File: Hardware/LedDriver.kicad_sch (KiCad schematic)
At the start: 10 parts

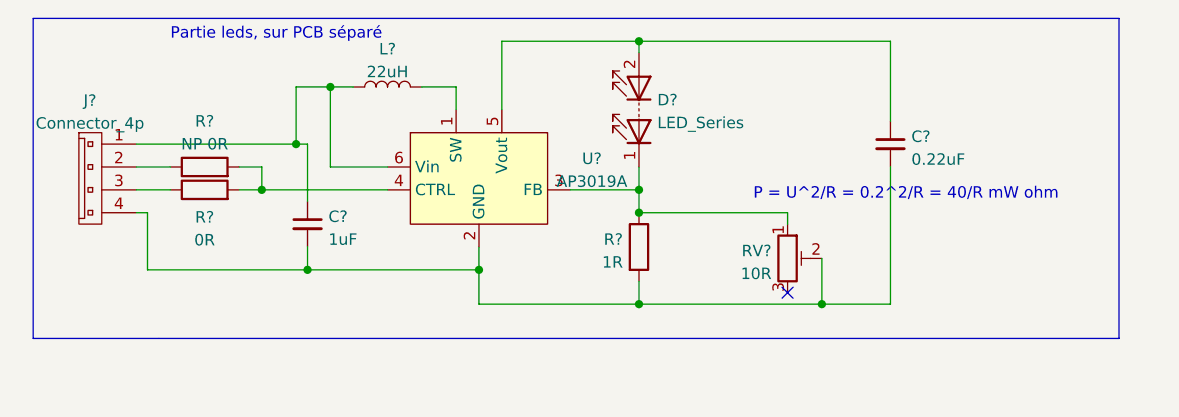
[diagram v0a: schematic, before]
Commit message: pcb led driver
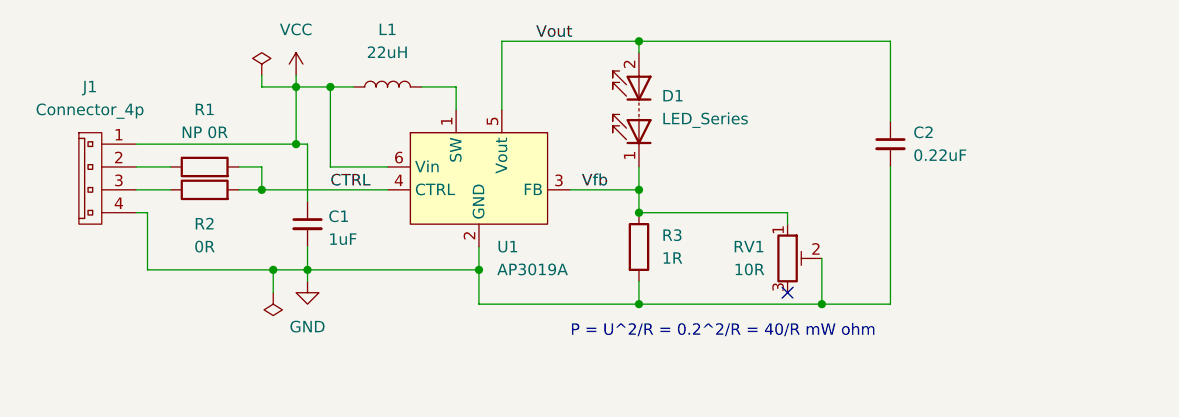
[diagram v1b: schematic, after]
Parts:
- C1, C2: renamed from C?; footprint (none) -> 0ESNLib:C_0805_2012Metric_Pad1.18x1.45mm_HandSolder
- D1: renamed from D?; footprint (none) -> 0ESNLib:D_0603_1608Metric_Pad1.05x0.95mm_HandSolder
- L1: renamed from L?; footprint (none) -> 0ESNLib:sumida_CDRH_inductor
- R1, R2, R3: renamed from R?; footprint (none) -> Resistor_SMD:R_0805_2012Metric_Pad1.20x1.40mm_HandSolder
- U1: renamed from U?; footprint (none) -> Package_TO_SOT_SMD:TSOT-23-6_HandSoldering
- gave numbers to parts that had none: 2
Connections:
- net Vfb: now reaches D1.1 (K), R3.1, RV1.1, U1.3 (FB)
- net GND: now reaches C1.2, C2.2, J1.4 (P4), R3.2, RV1.2, U1.2 (GND)
- net CTRL: now reaches R1.2, R2.2, U1.4 (CTRL)
- net Vout: now reaches C2.1, D1.2 (A), U1.5 (Vout)
- net VCC: now reaches C1.1, J1.1 (P1), L1.1, U1.6 (Vin)
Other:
- note removed: "Partie leds, sur PCB séparé"

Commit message: edited libraries
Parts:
- J1: value Connector_4p -> Led connector; footprint 0ESN_Lib:Connector_2p_m -> 0ESN_Lib:Connector_4p_m
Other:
- note added: "EN"
- note added: "GND"
- note added: "PWM"
- note added: "Vbat"
- moved on the sheet: C1, C2, D1, L1, R1, R2, R3, RV1, U1

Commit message: led driver schematic done
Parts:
- C1, C2: footprint 0ESNLib:C_0805_2012Metric_Pad1.18x1.45mm_HandSolder -> 0ESN_Lib:C_0805_2012Metric_Pad1.18x1.45mm_HandSolder
- D1: footprint 0ESNLib:D_0603_1608Metric_Pad1.05x0.95mm_HandSolder -> 0ESN_Lib:C_0805_2012Metric_Pad1.18x1.45mm_HandSolder
- L1: footprint 0ESNLib:sumida_CDRH_inductor -> 0ESN_Lib:sumida_CDRH_inductor
- RV1: footprint (none) -> 0ESN_Lib:Bourns_3362p_trimpot
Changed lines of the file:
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@@
       (effects (font (size 1.27 1.27)) (justify right))
     )
-    (property "Footprint" "" (id 2) (at 182.88 107.95 0)
+    (property "Footprint" "0ESN_Lib:Bourns_3362p_trimpot" (id 2) (at 182.88 107.95 0)
       (effects (font (size 1.27 1.27)) hide)
     )
@@
     (property "Reference" "L1" (id 0) (at 139.7 83.82 90))
     (property "Value" "22uH" (id 1) (at 139.7 86.36 90))
-    (property "Footprint" "0ESNLib:sumida_CDRH_inductor" (id 2) (at 139.7 90.17 0)
+    (property "Footprint" "0ESN_Lib:sumida_CDRH_inductor" (id 2) (at 139.7 90.17 0)
       (effects (font (size 1.27 1.27)) hide)
     )
@@
       (effects (font (size 1.27 1.27)) (justify right))
     )
-    (property "Footprint" "0ESNLib:D_0603_1608Metric_Pad1.05x0.95mm_HandSolder" (id 2) (at 166.37 95.25 0)
+    (property "Footprint" "0ESN_Lib:C_0805_2012Metric_Pad1.18x1.45mm_HandSolder" (id 2) (at 166.37 95.25 0)
       (effects (font (size 1.27 1.27)) hide)
     )
@@
       (effects (font (size 1.27 1.27)) (justify left))
     )
-    (property "Footprint" "0ESNLib:C_0805_2012Metric_Pad1.18x1.45mm_HandSolder" (id 2) (at 129.54 105.41 0)
+    (property "Footprint" "0ESN_Lib:C_0805_2012Metric_Pad1.18x1.45mm_HandSolder" (id 2) (at 129.54 105.41 0)
       (effects (font (size 1.27 1.27)) hide)
     )
@@
       (effects (font (size 1.27 1.27)) (justify left))
     )
-    (property "Footprint" "0ESNLib:C_0805_2012Metric_Pad1.18x1.45mm_HandSolder" (id 2) (at 194.31 100.33 0)
+    (property "Footprint" "0ESN_Lib:C_0805_2012Metric_Pad1.18x1.45mm_HandSolder" (id 2) (at 194.31 100.33 0)
       (effects (font (size 1.27 1.27)) hide)
     )
@@
     )
     (path "/be7fe3ef-4c8c-4441-a8b1-9f6c4a556dbd"
-      (reference "C1") (unit 1) (value "1uF") (footprint "0ESNLib:C_0805_2012Metric_Pad1.18x1.45mm_HandSolder")
+      (reference "C1") (unit 1) (value "1uF") (footprint "0ESN_Lib:C_0805_2012Metric_Pad1.18x1.45mm_HandSolder")
     )
     (path "/cabd8106-febf-4c1c-a427-4a77d8f3282a"
-      (reference "C2") (unit 1) (value "0.22uF") (footprint "0ESNLib:C_0805_2012Metric_Pad1.18x1.45mm_HandSolder")
+      (reference "C2") (unit 1) (value "0.22uF") (footprint "0ESN_Lib:C_0805_2012Metric_Pad1.18x1.45mm_HandSolder")
     )
     (path "/b9fa4c1e-5267-4696-a1ce-f87e6baeeb29"
-      (reference "D1") (unit 1) (value "LED_Series") (footprint "0ESNLib:D_0603_1608Metric_Pad1.05x0.95mm_HandSolder")
+      (reference "D1") (unit 1) (value "LED_Series") (footprint "0ESN_Lib:C_0805_2012Metric_Pad1.18x1.45mm_HandSolder")
     )
     (path "/e4ceb904-3dd0-416a-906e-cac55e2455db"
@@
     )
     (path "/9c08c45f-ba32-4b2b-8fe9-de49dcdc4262"
-      (reference "L1") (unit 1) (value "22uH") (footprint "0ESNLib:sumida_CDRH_inductor")
+      (reference "L1") (unit 1) (value "22uH") (footprint "0ESN_Lib:sumida_CDRH_inductor")
     )
     (path "/a5b92ca1-98a4-4608-b742-8ab56d6b3726"
@@
     )
     (path "/0229117d-4c4e-4f89-956e-fd71503672e7"
-      (reference "RV1") (unit 1) (value "10R") (footprint "")
+      (reference "RV1") (unit 1) (value "10R") (footprint "0ESN_Lib:Bourns_3362p_trimpot")
     )
     (path "/17354649-0d95-44b1-afcb-6c3c12f701a5"

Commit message: led driver pcb complete
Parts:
- D1: footprint 0ESN_Lib:C_0805_2012Metric_Pad1.18x1.45mm_HandSolder -> 0ESN_Lib:Wire_2x2; symbol Device:LED_Series -> 0ESN_Lib:LED_Series
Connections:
- net Vfb: now also D1.2 (K); no longer D1.1 (K)
- net Vout: now also D1.1 (A); no longer D1.2 (A)
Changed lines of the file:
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@@
     (pin "1")
   )
-  (symbol (lib_id "Device:LED_Series") (at 166.37 92.71 90) (unit 1)
+  (symbol (lib_id "0ESN_Lib:LED_Series") (at 166.37 92.71 90) (unit 1)
     (in_bom yes) (on_board yes) (fields_autoplaced)
     (property "Reference" "D1" (id 0) (at 168.91 91.1859 90)
@@
       (effects (font (size 1.27 1.27)) (justify right))
     )
-    (property "Footprint" "0ESN_Lib:C_0805_2012Metric_Pad1.18x1.45mm_HandSolder" (id 2) (at 166.37 95.25 0)
+    (property "Footprint" "0ESN_Lib:Wire_2x2" (id 2) (at 166.37 95.25 0)
       (effects (font (size 1.27 1.27)) hide)
     )
@@
     )
     (path "/b9fa4c1e-5267-4696-a1ce-f87e6baeeb29"
-      (reference "D1") (unit 1) (value "LED_Series") (footprint "0ESN_Lib:C_0805_2012Metric_Pad1.18x1.45mm_HandSolder")
+      (reference "D1") (unit 1) (value "LED_Series") (footprint "0ESN_Lib:Wire_2x2")
     )
     (path "/e4ceb904-3dd0-416a-906e-cac55e2455db"

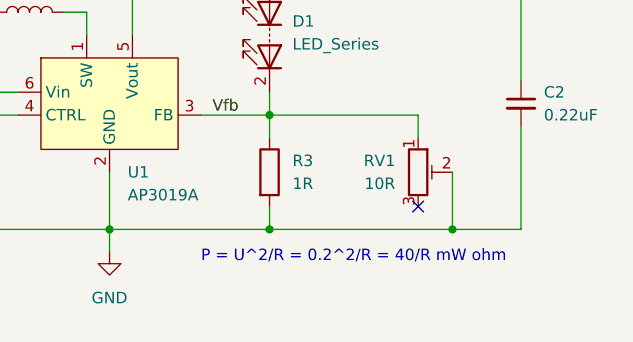
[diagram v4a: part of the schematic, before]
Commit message: schematic update
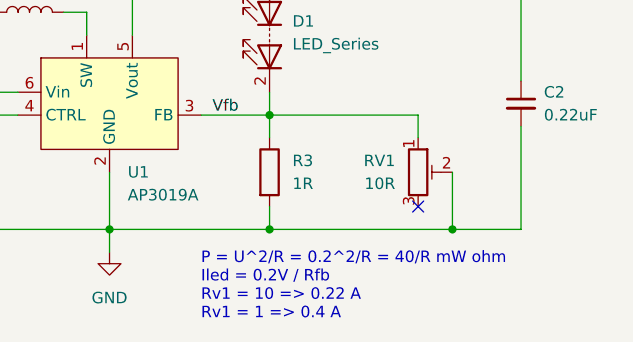
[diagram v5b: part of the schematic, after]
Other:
- note added: "P = U^2/R = 0.2^2/R = 40/R mW ohm Iled = 0.2V / Rfb Rv1 = 10 => 0.22 A Rv1 = 1 => 0.4 A"
- note removed: "P = U^2/R = 0.2^2/R = 40/R mW ohm"
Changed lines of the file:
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@@
     (effects (font (size 1.27 1.27)) (justify right bottom))
   )
-  (text "P = U^2/R = 0.2^2/R = 40/R mW ohm" (at 158.75 118.11 0)
+  (text "P = U^2/R = 0.2^2/R = 40/R mW ohm\nIled = 0.2V / Rfb\nRv1 = 10 => 0.22 A\nRv1 = 1 => 0.4 A"
+    (at 158.75 124.46 0)
     (effects (font (size 1.27 1.27)) (justify left bottom))
   )
